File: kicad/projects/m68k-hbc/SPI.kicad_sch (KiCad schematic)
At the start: 1 part, among them U3 TP3465V

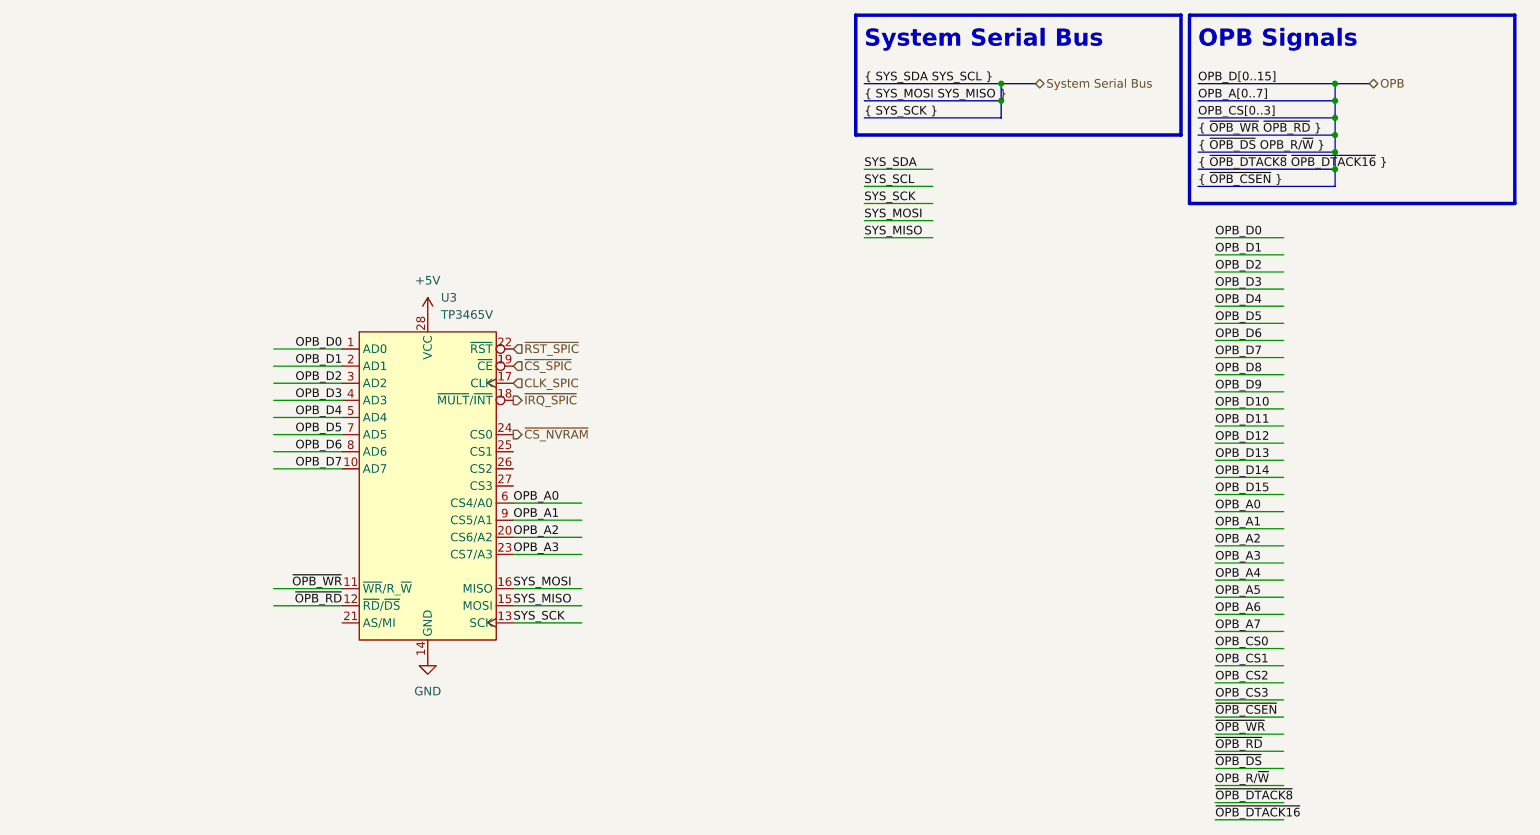
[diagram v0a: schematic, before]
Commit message: Large changes: EHBCSimpleEmu, kicad, fwcode, docs
This commit contains some large changes:
- Removed EHBCSimpleEmu (Moved to kms1212/llemu, kms1212/qemu)
- (likely) Removed fwcode; now it only boots and stops
- Modified documents
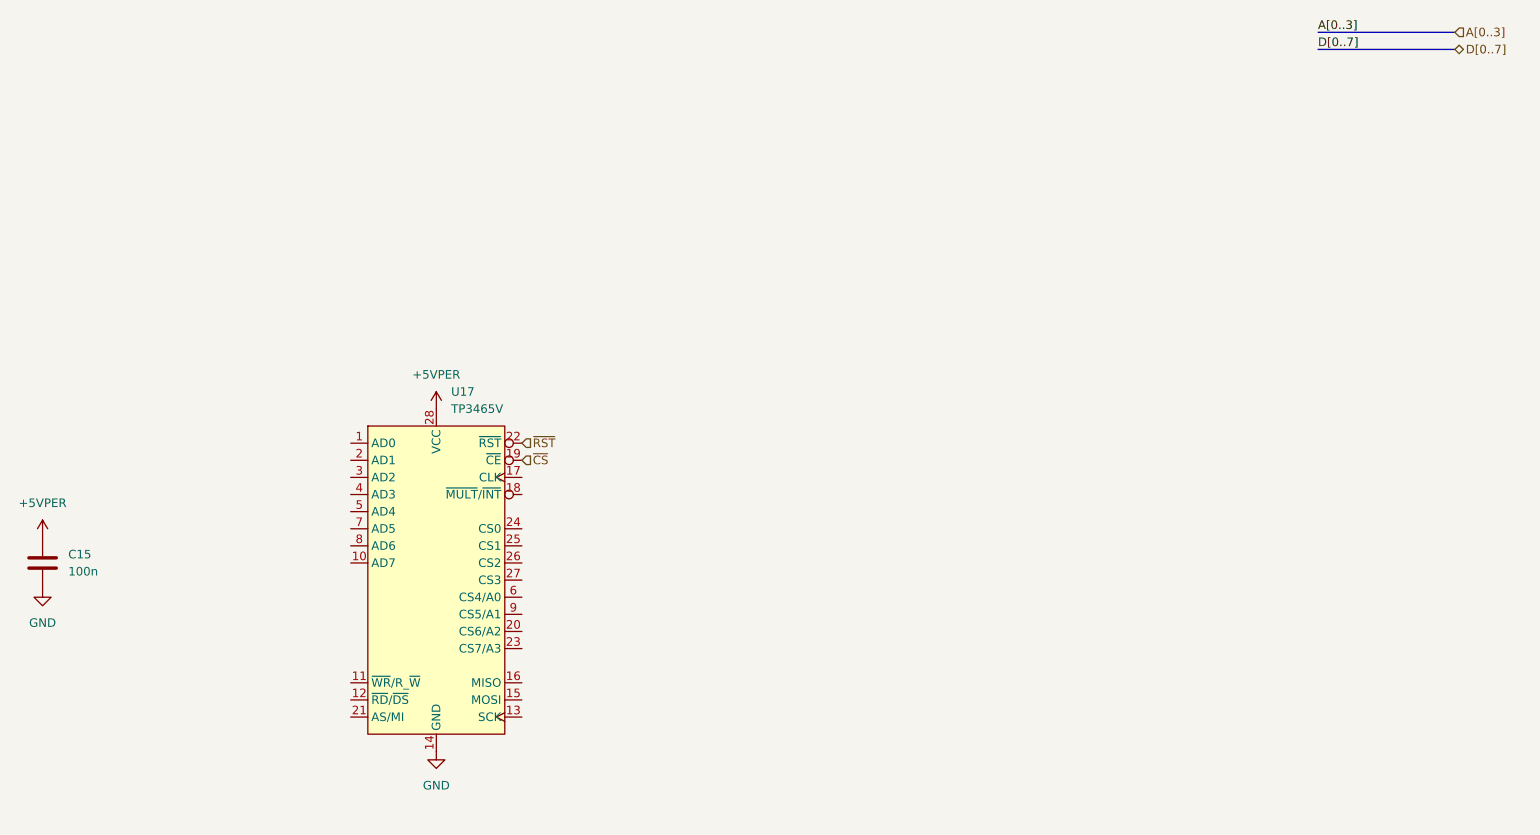
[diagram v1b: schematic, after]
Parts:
- removed U3: TP3465V, Package_LCC:PLCC-28, symbol m68k-hbc-ic:TP3465V
- added C15: 100n, Capacitor_THT:C_Disc_D6.0mm_W2.5mm_P5.00mm, symbol Device:C
- added U17: TP3465V, Package_LCC:PLCC-28_THT-Socket, symbol m68k-hbc-ic:TP3465V
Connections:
- net GND: now also C15.2, U17.14 (GND)
- new net +5VPER: C15.1, U17.28 (VCC)
- new net ~{CS}: U17.19 (~{CE})
- new net ~{RST}: U17.22 (~{RST})
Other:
- note removed: "OPB Signals"
- note removed: "System Serial Bus"
